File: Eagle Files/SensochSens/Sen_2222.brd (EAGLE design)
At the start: 63.5 x 50.5 mm, 36 parts, among them U1 SM700PC1SMD, U2 MIC5219, U3 KCSA03-102SMD_7SEG

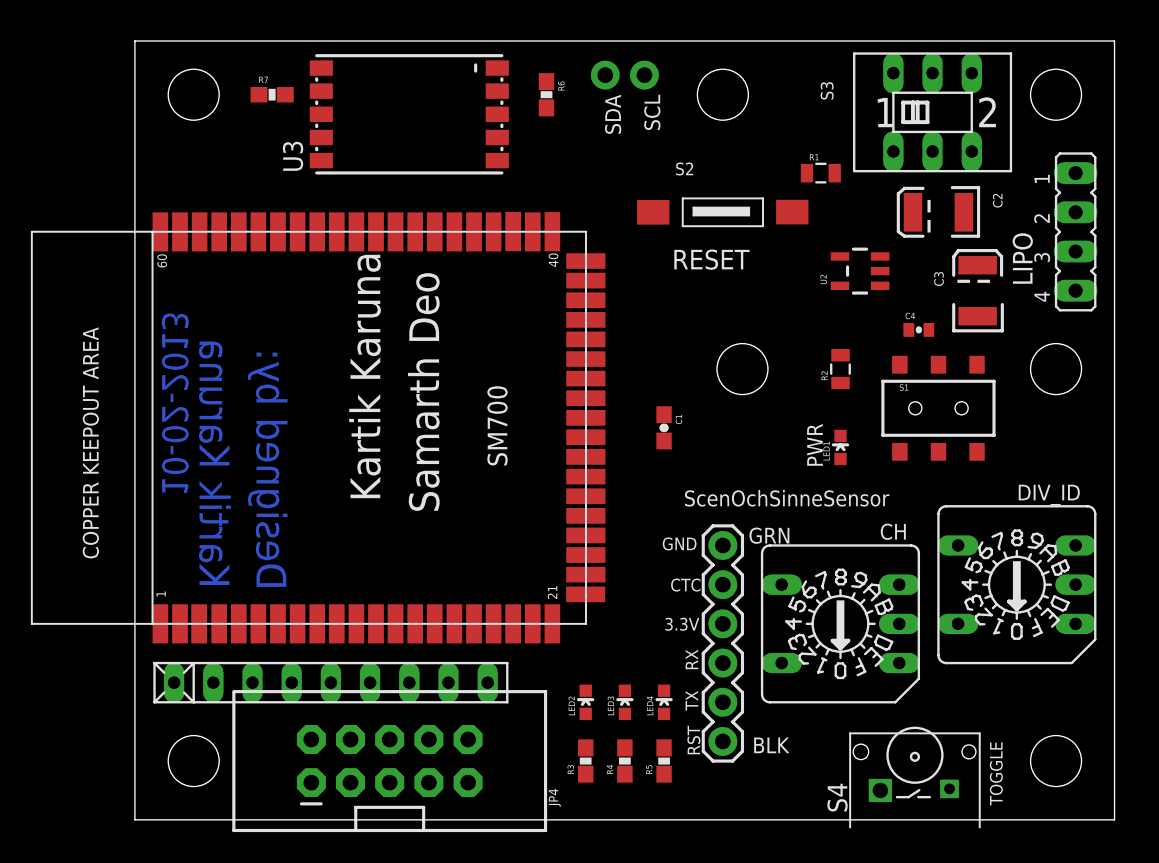
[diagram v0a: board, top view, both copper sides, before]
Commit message: 
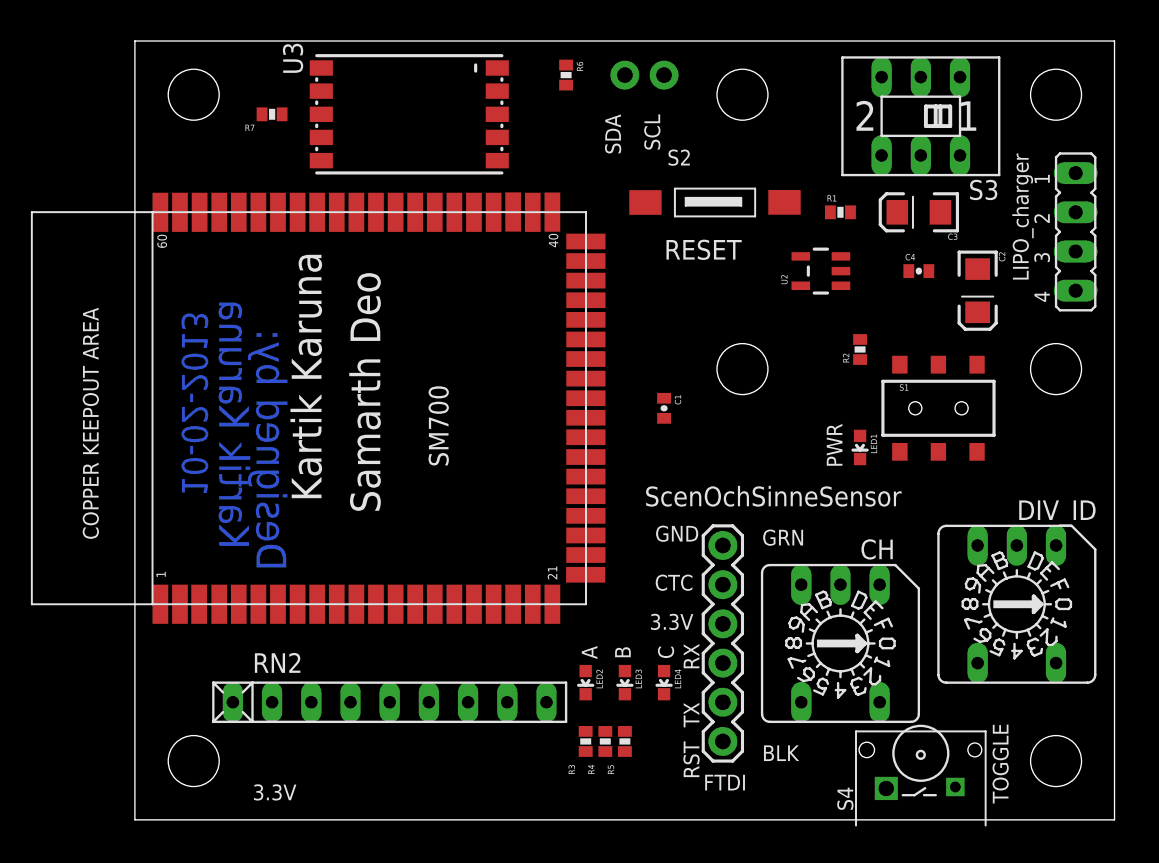
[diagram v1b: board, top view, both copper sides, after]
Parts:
- removed JP11: STAND-OFF, SparkFun:STAND-OFF
- C1: device SparkFun-Passives:0603-CAP -> SparkFun-Passives:0402-CAP
- C2, C3: device SparkFun-Passives:EIA3528 -> SparkFun-Passives:EIA3216
- JP2: value LIPO -> LIPO_charger
- JP4: value M05X2SHD_LOCK -> STAND-OFF; device SparkFun-Connectors:2X5-SHROUDED_LOCK -> SparkFun:STAND-OFF
- R1, R2: device SparkFun-Passives:0805 -> SparkFun-Passives:0402-RES
- R3, R4, R5, R6, R7: device SparkFun-Passives:0603-RES -> SparkFun-Passives:0402-RES
- moved JP5 61.4 mm to (3.81, 3.81)
- moved JP8 61.4 mm to (59.7, 29.2)
- moved JP7 43.2 mm to (59.7, 47.0)
- moved JP4 43.2 mm to (59.7, 3.81), turned to 0 degrees
- moved JP6 39.8 mm to (3.81, 47.0)
- moved JP9 35.6 mm to (39.4, 47.0)
- moved JP10 17.8 mm to (39.4, 29.2)
- moved C3 6.35 mm to (50.8, 39.4), turned to 180 degrees
- moved C2 5.68 mm to (54.6, 34.3), turned to 270 degrees
- moved RN2 4.02 mm to (16.5, 7.62)
- moved C4 3.81 mm to (50.8, 35.6)
- moved R5 2.84 mm to (31.8, 5.08)
- moved R1 2.84 mm to (45.7, 39.4)
- moved U2 2.54 mm to (44.5, 35.6)
- moved R2 1.80 mm to (47.0, 30.5)
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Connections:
- net 3.3V: no longer JP4.1, JP4.10
- net ADC0: no longer JP4.2
- net ADC1: no longer JP4.3
- net ADC2: no longer JP4.4
- net ADC3: no longer JP4.5
- net ADC4: no longer JP4.6
- net ADC5: no longer JP4.7
- net ADC6: no longer JP4.8
- net ADC7: no longer JP4.9
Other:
- board text added: "A"
- board text added: "B"
- board text added: "C"
